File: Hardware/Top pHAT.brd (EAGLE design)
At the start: 85 x 56 mm, 77 parts, among them J1 QWIIC, J2 AVR_SPI_PROG_3X2TESTPOINTS, J3 2.4" TFT, Q2 1.1A/60V/600mΩ, U2 ADMP401, U3 ADMP401, U4 WM8960, U5 ATTINY84, Y1 24 MHz

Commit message: post checklist changes
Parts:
- S6: value (none) -> Joystick
- U1: value (none) -> Raspberry Pi Header
- moved TP7 1.27 mm to (59.7, 7.62)
- moved I2C 1.00 mm to (73.5, 5.00)
- moved U$8 0.90 mm to (71.5, 6.60)
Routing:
- net D/C: track 40.1 -> 39.0 mm
- net 3.3V: track 194.1 -> 193.1 mm
- net N$17: track 3.59 -> 4.53 mm
- net SDO: track 30.6 -> 31.5 mm
- net N$16: track 4.80 -> 5.59 mm
- net LED_DATA: track 57.6 -> 58.1 mm

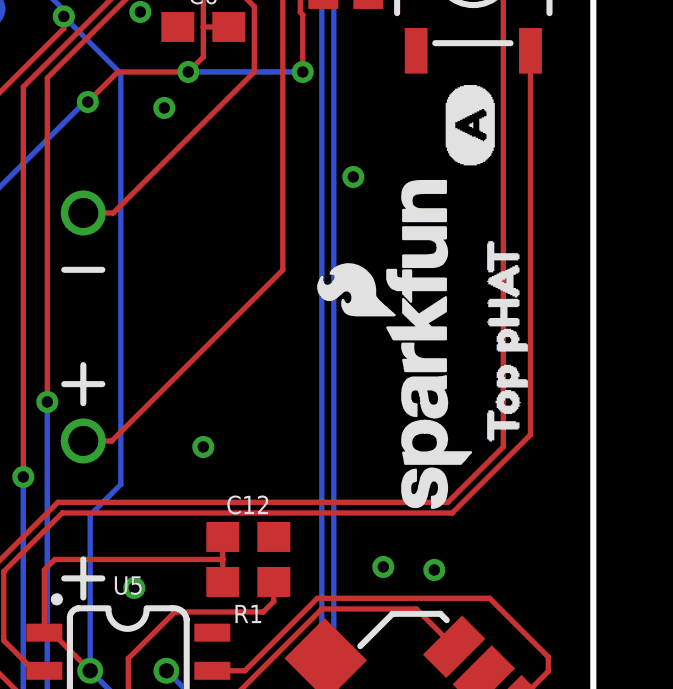
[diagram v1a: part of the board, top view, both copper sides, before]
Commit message: adding top pHAT silk
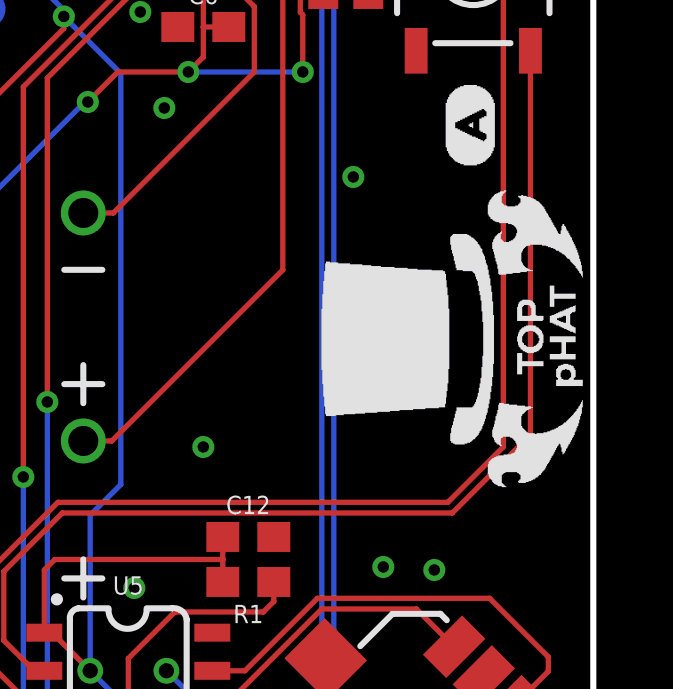
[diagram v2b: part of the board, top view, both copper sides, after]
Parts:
- removed LOGO1: SFE_LOGO_NAME_FLAME.1_INCH, SparkFun-Aesthetics:SFE_LOGO_NAME_FLAME_.1
- removed U$2: (no value), buzzard_labels (21):TOP_PHAT0
- added U$12: (no value), 2020#02#27#png (1):2020#02#27#PNG
- U$1: device buzzard_labels (21):_TOP_PHAT1 -> 2020#02#27#png (3):2020#02#27#PNG
- moved U$1 27.0 mm to (80.5, 27.0), flipped to the top, turned to 90 degrees
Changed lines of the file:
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@@
 <setting verticaltext="up"/>
 </settings>
-<grid distance="0.05" unitdist="inch" unit="inch" style="lines" multiple="1" display="yes" altdistance="0.1" altunitdist="mm" altunit="mm"/>
+<grid distance="0.05" unitdist="inch" unit="mm" style="lines" multiple="1" display="yes" altdistance="0.1" altunitdist="mm" altunit="mm"/>
 <layers>
 <layer number="1" name="Top" color="4" fill="1" visible="yes" active="yes"/>
@@
 <attribute name="VALUE" value="2.4&quot; TFT" x="19" y="28.9" size="1.778" layer="28" rot="MR90" display="off"/>
 </element>
-<element name="LOGO1" library="SparkFun-Aesthetics" package="SFE_LOGO_NAME_FLAME_.1" value="SFE_LOGO_NAME_FLAME.1_INCH" x="79.5" y="27" smashed="yes" rot="R90"/>
 <element name="LOGO2" library="SparkFun-Aesthetics" package="SFE_LOGO_NAME_FLAME_.4" value="SFE_LOGO_NAME_FLAME.4_INCH" x="67" y="21" smashed="yes" rot="MR0"/>
 <element name="LOGO3" library="SparkFun-Aesthetics" package="QWIIC_4MM" value="QWIIC_LOGO_4MM" x="78.5" y="7" smashed="yes"/>
@@
 <attribute name="VALUE" x="63.238" y="44.5" size="0.6096" layer="27" font="vector" ratio="20" rot="R270" align="top-center"/>
 </element>
-<element name="U$2" library="buzzard_labels (21)" package="TOP_PHAT0" value="" x="82" y="22.8" smashed="yes" rot="R90"/>
-<element name="U$1" library="buzzard_labels (21)" package="_TOP_PHAT1" value="" x="54" y="22" smashed="yes" rot="MR0"/>
 <element name="Q2" library="SparkFun-DiscreteSemi" package="SOT23-3" value="1.1A/60V/600mΩ" x="63" y="36" smashed="yes" rot="R270">
 <attribute name="NAME" x="63" y="37.651" size="0.6096" layer="25" font="vector" ratio="20" align="bottom-center"/>
@@
 <element name="U$10" library="buzzard_labels (22)" package="44" value="" x="15.6" y="2.2" smashed="yes" rot="R90"/>
 <element name="U$11" library="buzzard_labels (22)" package="55" value="" x="6.6" y="2.2" smashed="yes" rot="R90"/>
+<element name="U$12" library="2020#02#27#png (1)" package="2020#02#27#PNG" value="" x="43.18" y="15.24" smashed="yes" rot="MR0"/>
+<element name="U$1" library="2020#02#27#png (3)" package="2020#02#27#PNG" value="" x="80.5" y="27" smashed="yes" rot="R90"/>
 </elements>
 <signals>

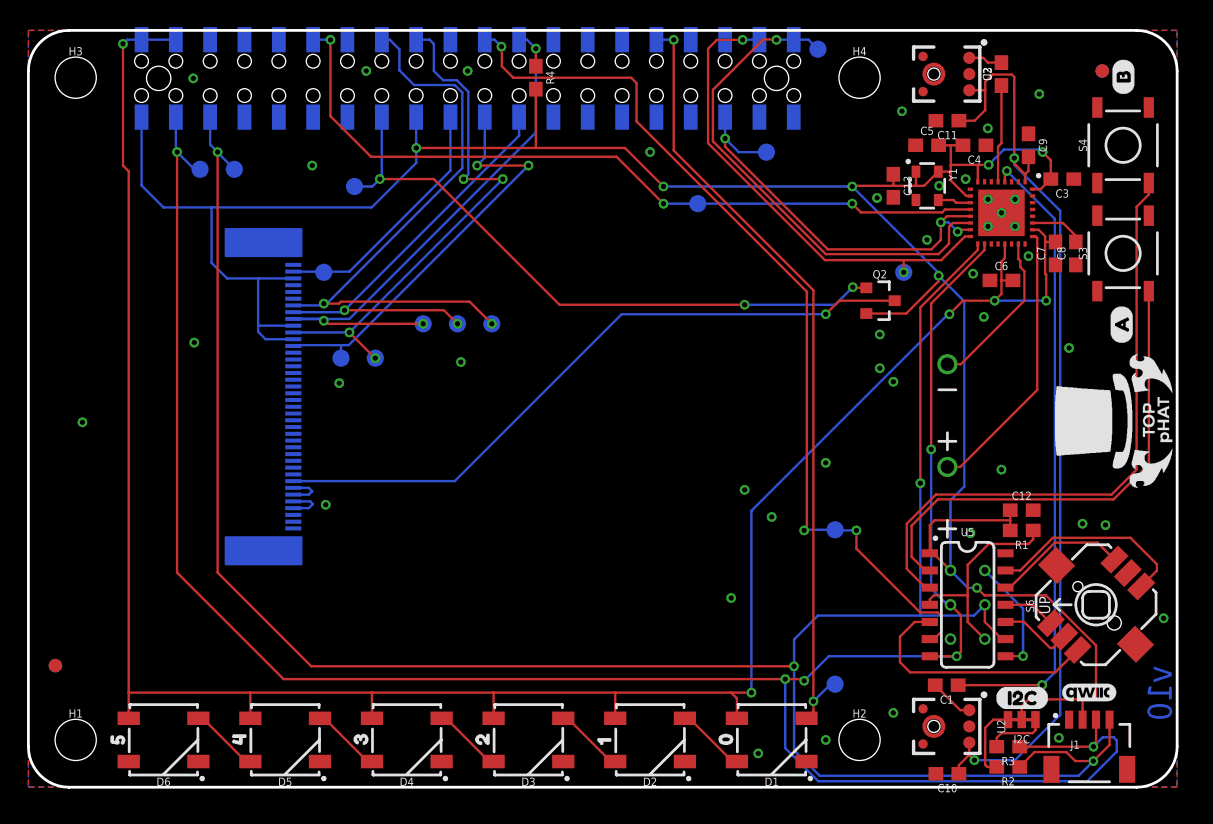
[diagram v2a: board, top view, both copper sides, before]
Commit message: v11 - mic and vector buzzards/graphics
-swapped out the mic for the ICS-40180
-updated labels to new vector buzzards
-converted top phat logo into vector version, currently in mini library.
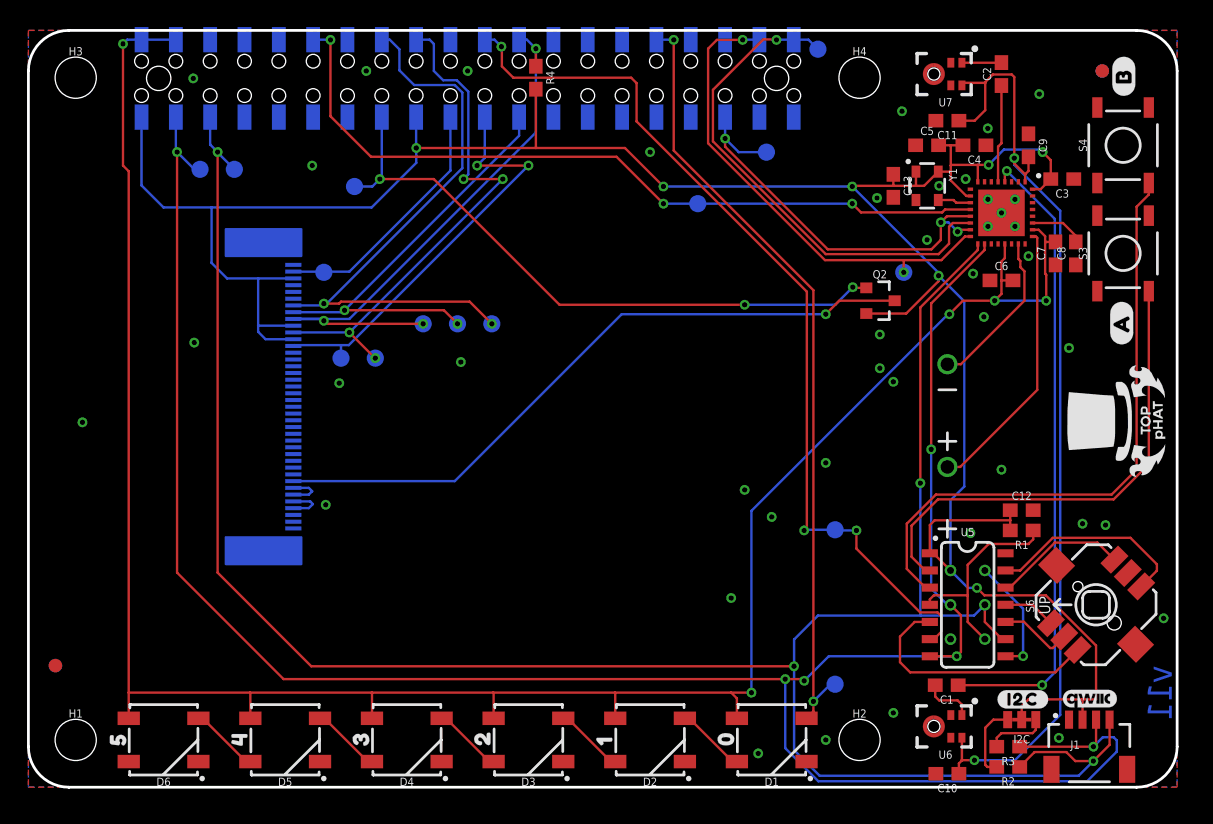
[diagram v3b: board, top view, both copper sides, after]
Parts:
- removed U$1: (no value), 2020#02#27#png (3):2020#02#27#PNG
- removed U$10: (no value), buzzard_labels (22):44
- removed U$11: (no value), buzzard_labels (22):55
- removed U$12: (no value), 2020#02#27#png (1):2020#02#27#PNG
- removed U$5: (no value), buzzard_labels (22):22
- removed U$9: (no value), buzzard_labels (22):33
- removed U2, U3: ADMP401, SparkFun-Sensors:ADMP401
- added U$13: (no value), output:10
- added U$14: (no value), output:20
- added U$15: (no value), output:30
- added U$16: (no value), output:40
- added U$17: (no value), output:50
- added U$2: (no value), output:#B#0
- added U6, U7: ICS40180, ICS-40180:ICS40180
- U$3: device buzzard_labels (22):00 -> top_phat_logo:TOP_PHAT_LOGO_1
- U$4: device buzzard_labels (22):11 -> top_phat_logo:TOP_PHAT_LOGO_SMALL
- U$6: device buzzard_labels (16):A0 -> output:#I2C#0
- U$7: device buzzard_labels (16):B1 -> output:#A#0
- U$8: device buzzard_labels (17):I2C3 -> output:00
- moved U$4 45.4 mm to (80.6, 27.1)
- moved U$6 27.3 mm to (73.6, 6.50), turned to 0 degrees
- moved U$8 20.1 mm to (51.6, 3.63), turned to 90 degrees
- moved U$7 16.8 mm to (80.9, 34.3)
- moved U$3 15.5 mm to (43.2, 15.2), flipped to the bottom, turned to 0 degrees
- moved LOGO3 0.46 mm to (78.6, 6.54)
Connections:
- net GND: now also U6.2, U6.3, U6.4, U7.2, U7.3, U7.4; no longer U2.2, U2.4, U2.6, U3.2, U3.4, U3.6
- net LEFTMIC: now also U6.1; no longer U2.1
- net MICBIAS: now also U6.5, U7.5; no longer U2.5, U3.5
- net RIGHTMIC: now also U7.1; no longer U3.1
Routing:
- net MICBIAS: track 71.0 -> 72.1 mm
- net LEFTMIC: track 3.29 -> 3.83 mm
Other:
- board text added: "Revised by: Pete Lewis"
- board text added: "v11"
- board text removed: "v10"

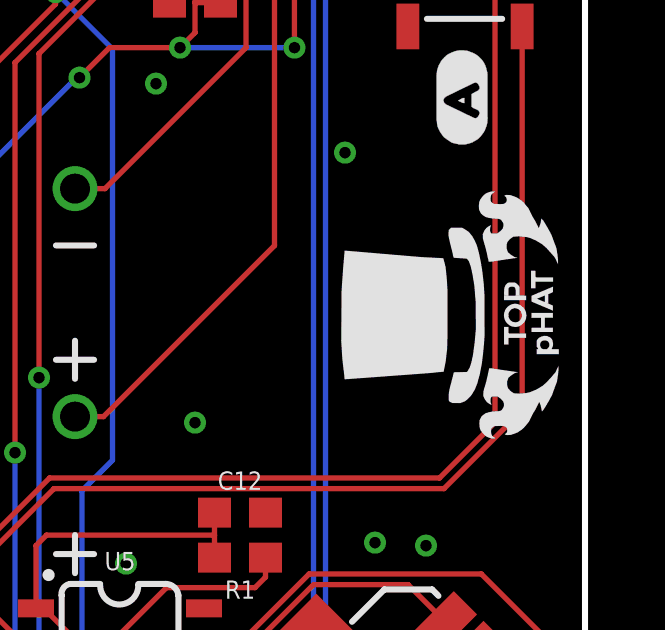
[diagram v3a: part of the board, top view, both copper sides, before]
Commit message: first run of checklist stuff
-CS net in schematic needed a nudge.
-enlarged top phat logo polygon lines to 0.0005"
-Added link to Qwiic Button repo in readme - for firmware and fusebits, if needed by user.
-added mic datasheet for good measure.
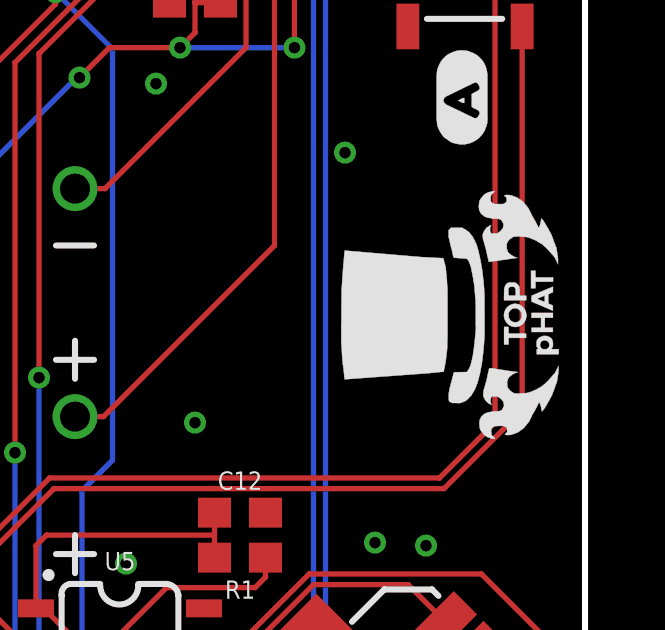
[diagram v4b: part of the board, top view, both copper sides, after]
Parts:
- removed U$3: (no value), top_phat_logo:TOP_PHAT_LOGO_1
- added U$1: (no value), top_phat_logo:TOP_PHAT_LOGO_BIG
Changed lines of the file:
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@@
 <drawing>
 <settings>
-<setting alwaysvectorfont="no"/>
+<setting alwaysvectorfont="yes"/>
 <setting verticaltext="up"/>
 </settings>
@@
 <element name="U$16" library="output" package="40" value="" x="15.621" y="3.6068" smashed="yes" rot="R90"/>
 <element name="U$17" library="output" package="50" value="" x="6.6548" y="3.5814" smashed="yes" rot="R90"/>
-<element name="U$3" library="top_phat_logo" package="TOP_PHAT_LOGO_1" value="" x="43.18" y="15.24" smashed="yes" rot="MR0"/>
 <element name="U$4" library="top_phat_logo" package="TOP_PHAT_LOGO_SMALL" value="" x="80.645" y="27.051" smashed="yes" rot="R90"/>
+<element name="U$1" library="top_phat_logo" package="TOP_PHAT_LOGO_BIG" value="" x="43.18" y="15.24" smashed="yes" rot="MR0"/>
 </elements>
 <signals>
